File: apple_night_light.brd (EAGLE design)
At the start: 100 x 55 mm, 39 parts, among them U2 INA219AIDCNR, U3 ATSHA204-TSU, Y1 16MHZ

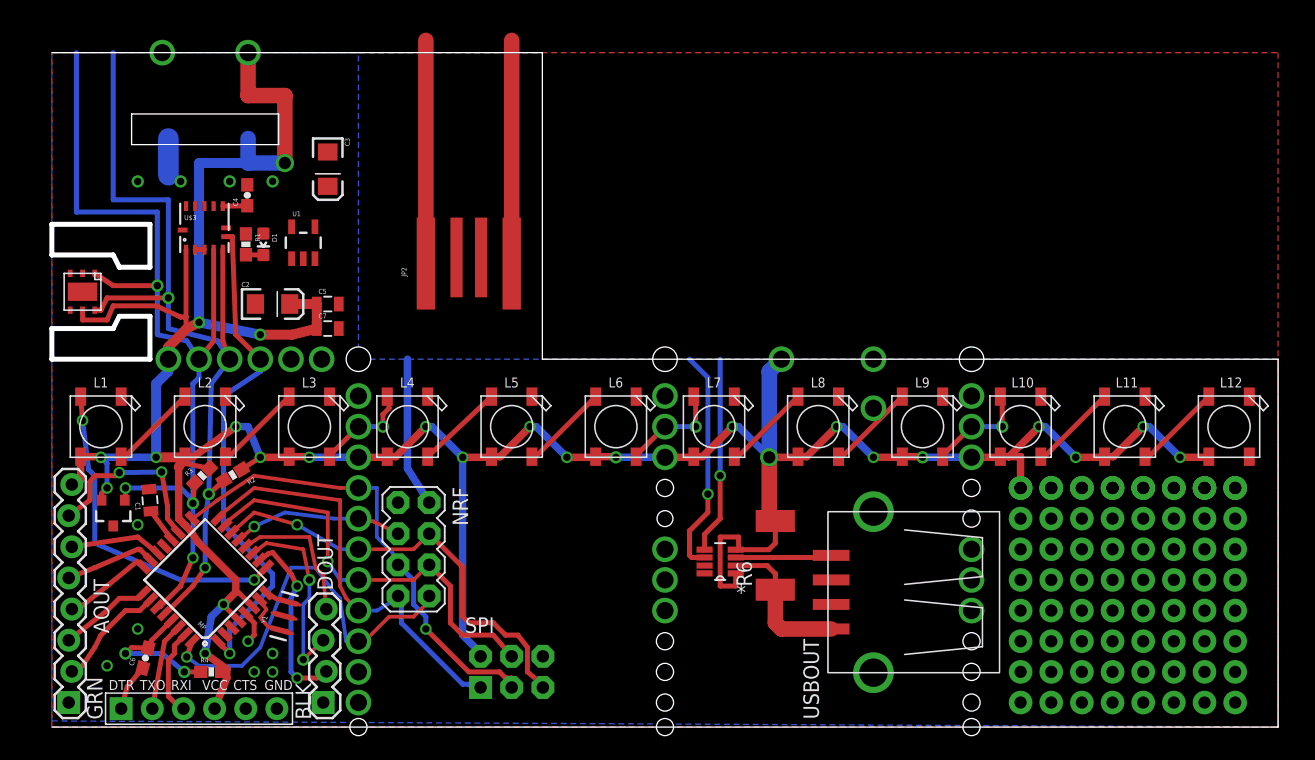
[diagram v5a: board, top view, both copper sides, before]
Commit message: layout power, move usb connector to save money, trying to finalize
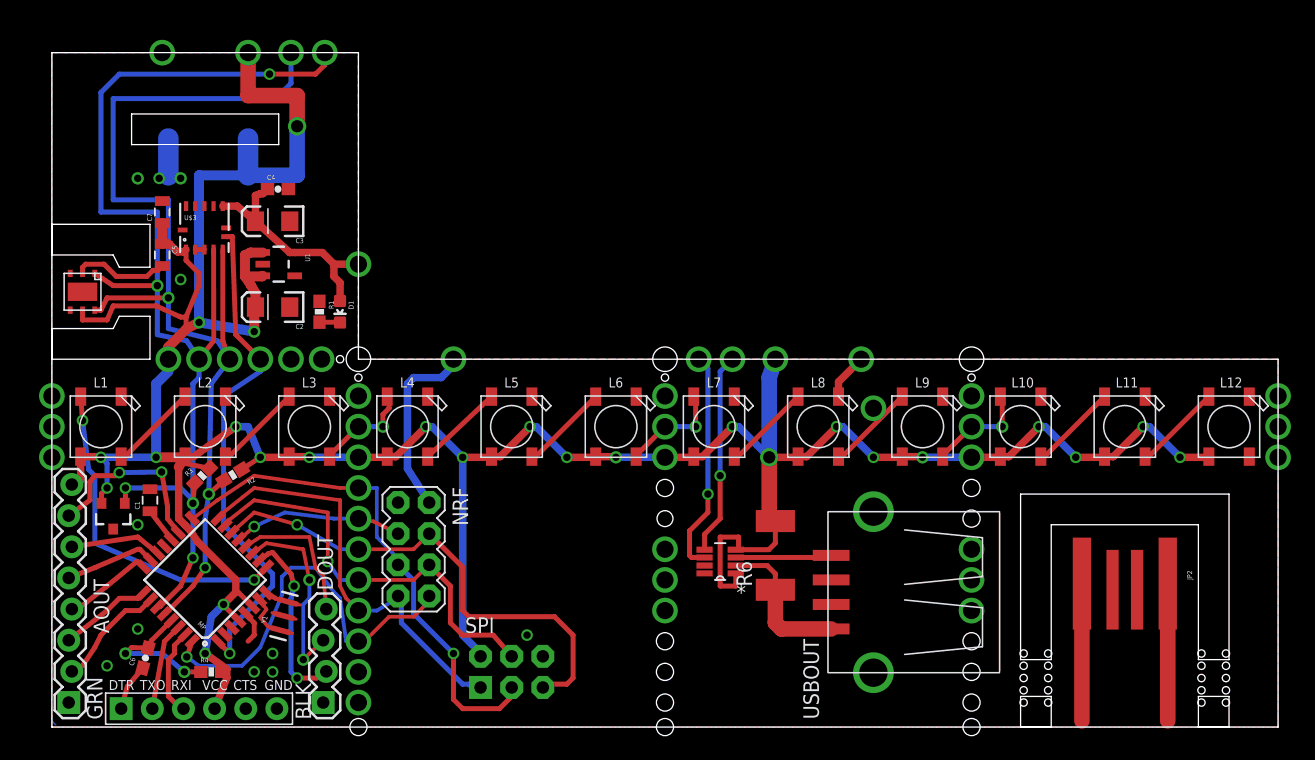
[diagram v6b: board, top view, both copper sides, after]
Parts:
- moved JP2 59.7 mm to (87.5, 11.5), turned to 270 degrees
- moved C7 16.5 mm to (9.00, 42.0), turned to 90 degrees
- moved C5 14.1 mm to (9.00, 38.5), turned to 270 degrees
- moved D1 8.33 mm to (23.5, 33.9)
- moved R1 8.14 mm to (21.8, 33.9)
- moved C3 6.19 mm to (18.0, 41.2), turned to 180 degrees
- moved U1 2.66 mm to (18.5, 37.8), turned to 270 degrees
- moved C4 2.55 mm to (18.4, 43.9), turned to 0 degrees
- moved C2 0.25 mm to (18.0, 34.2), turned to 180 degrees
- moved U3 0.25 mm to (5.00, 17.2)
- turned C1 to 90 degrees
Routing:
- net +3V3: track 14.2 -> 34.4 mm, vias 0 -> 2
- net SDA: track 97.5 -> 112.4 mm, vias 6 -> 9
- net SCL: track 88.9 -> 103.1 mm, vias 5 -> 7
- net CSN: track 36.1 -> 41.4 mm
- net GND: track 32.7 -> 37.4 mm, vias 33 -> 32
- net SCK: track 38.7 -> 42.2 mm
- net +5V: track 291.4 -> 288.5 mm, vias 33 -> 31
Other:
- outline, holes or cut-outs redrawn

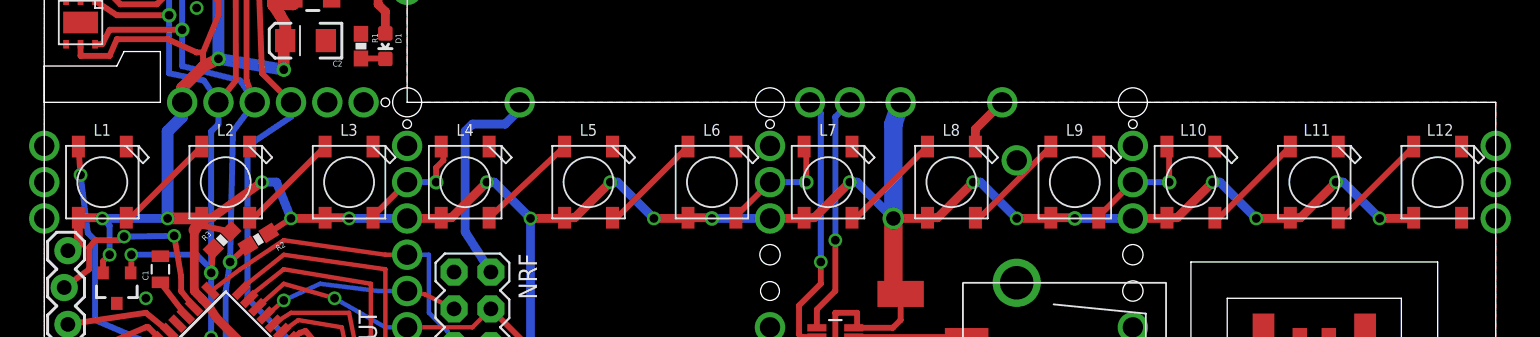
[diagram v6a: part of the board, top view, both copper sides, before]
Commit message: converting to dotstar LEDs, still some hookup work needed
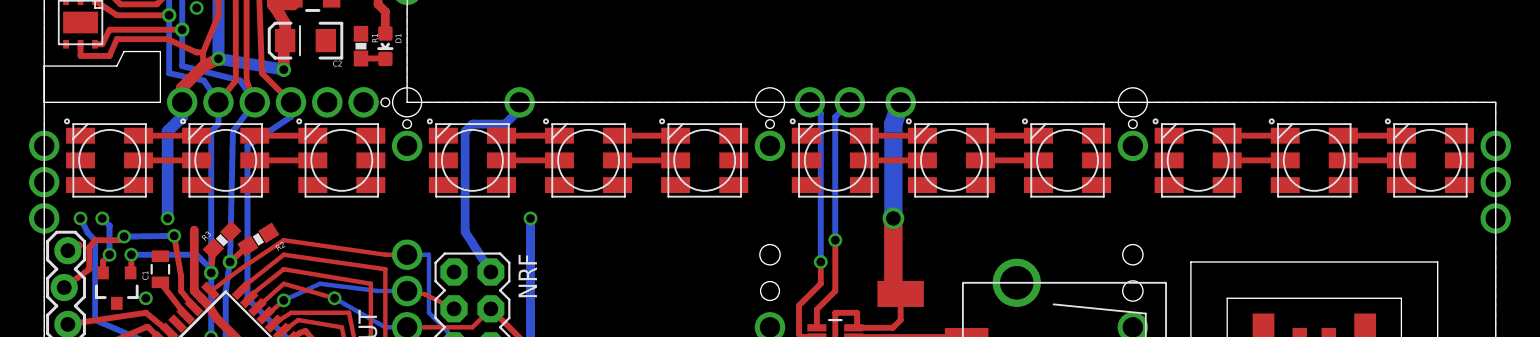
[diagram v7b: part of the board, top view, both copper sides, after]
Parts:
- removed L1, L10, L11, L12, L2, L3, L4, L5, L6, L7, L8, L9: WS2812B, adafruit:WS2812B
- added LED1, LED10, LED11, LED12, LED2, LED3, LED4, LED5, LED6, LED7, LED8, LED9: RGBLED5050, adafruit:RGBLED5050
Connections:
- removed net N$14: L5.2-DOUT, L6.4-DIN
- removed net N$20: L7.2-DOUT, L8.4-DIN
- removed net N$28: L4.2-DOUT, L5.4-DIN
- new net APACI: LED1.5
- new net APACI1: LED3.2, LED4.5
- new net APACI2: LED6.2, LED7.5
- new net APACI3: LED10.5, LED9.2
- new net APADI: LED1.4
- new net N$1: LED1.2, LED2.5
- new net N$15: LED4.2, LED5.5
- new net N$18: LED4.3, LED5.4
- new net N$26: LED8.3, LED9.4
- new net N$30: LED10.2, LED11.5
- new net N$31: LED11.2, LED12.5
- new net N$32: LED10.3, LED11.4
- new net N$35: LED11.3, LED12.4
- new net N$5: LED2.3, LED3.4
- new net N$6: LED3.3, LED4.4
- new net N$8: LED6.3, LED7.4
- net +5V: now also LED1.1, LED10.1, LED11.1, LED12.1, LED2.1, LED3.1, LED4.1, LED5.1, LED6.1, LED7.1, LED8.1, LED9.1; no longer L1.1-VDD, L10.1-VDD, L11.1-VDD, L12.1-VDD, L2.1-VDD, L3.1-VDD, L4.1-VDD, L5.1-VDD, L6.1-VDD, L7.1-VDD, L8.1-VDD, L9.1-VDD
- net GND: now also LED1.6, LED10.6, LED11.6, LED12.6, LED2.6, LED3.6, LED4.6, LED5.6, LED6.6, LED7.6, LED8.6, LED9.6; no longer L1.3-GND, L10.3-GND, L11.3-GND, L12.3-GND, L2.3-GND, L3.3-GND, L4.3-GND, L5.3-GND, L6.3-GND, L7.3-GND, L8.3-GND, L9.3-GND
- net N$12: now also LED10.4, LED9.3; no longer L6.2-DOUT, L7.4-DIN
- net N$17: now also LED5.2, LED6.5; no longer L10.4-DIN, L9.2-DOUT
- net N$19: now also LED5.3, LED6.4; no longer L8.2-DOUT, L9.4-DIN
- net N$2: now also LED2.2, LED3.5; no longer L2.2-DOUT, L3.4-DIN
- net N$23: now also LED7.2, LED8.5; no longer L3.2-DOUT, L4.4-DIN
- net N$24: now also LED8.2, LED9.5; no longer L11.2-DOUT, L12.4-DIN
- net N$25: now also LED7.3, LED8.4; no longer L10.2-DOUT, L11.4-DIN
- net N$3: now also LED1.3, LED2.4; no longer L1.2-DOUT, L2.4-DIN
- net NPIN: no longer L1.4-DIN
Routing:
- net +5V: track 288.5 -> 173.8 mm, vias 31 -> 13
- net N$12: track 8.49 -> 0.00 mm, vias 2 -> 0
- net N$20: track 7.23 -> 0.00 mm
- net N$14: track 7.23 -> 0.00 mm
- net N$28: track 7.14 -> 0.00 mm
- net NPIN: track 27.3 -> 22.4 mm
- net N$17: track 8.64 -> 4.00 mm, vias 2 -> 0
- net N$23: track 8.14 -> 4.00 mm, vias 2 -> 0
- net N$5: track 0.00 -> 4.00 mm
- net N$35: track 0.00 -> 4.00 mm
- net N$32: track 0.00 -> 4.00 mm
- net N$31: track 0.00 -> 4.00 mm
- net N$30: track 0.00 -> 4.00 mm
- net N$26: track 0.00 -> 4.00 mm
- net N$18: track 0.00 -> 4.00 mm
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
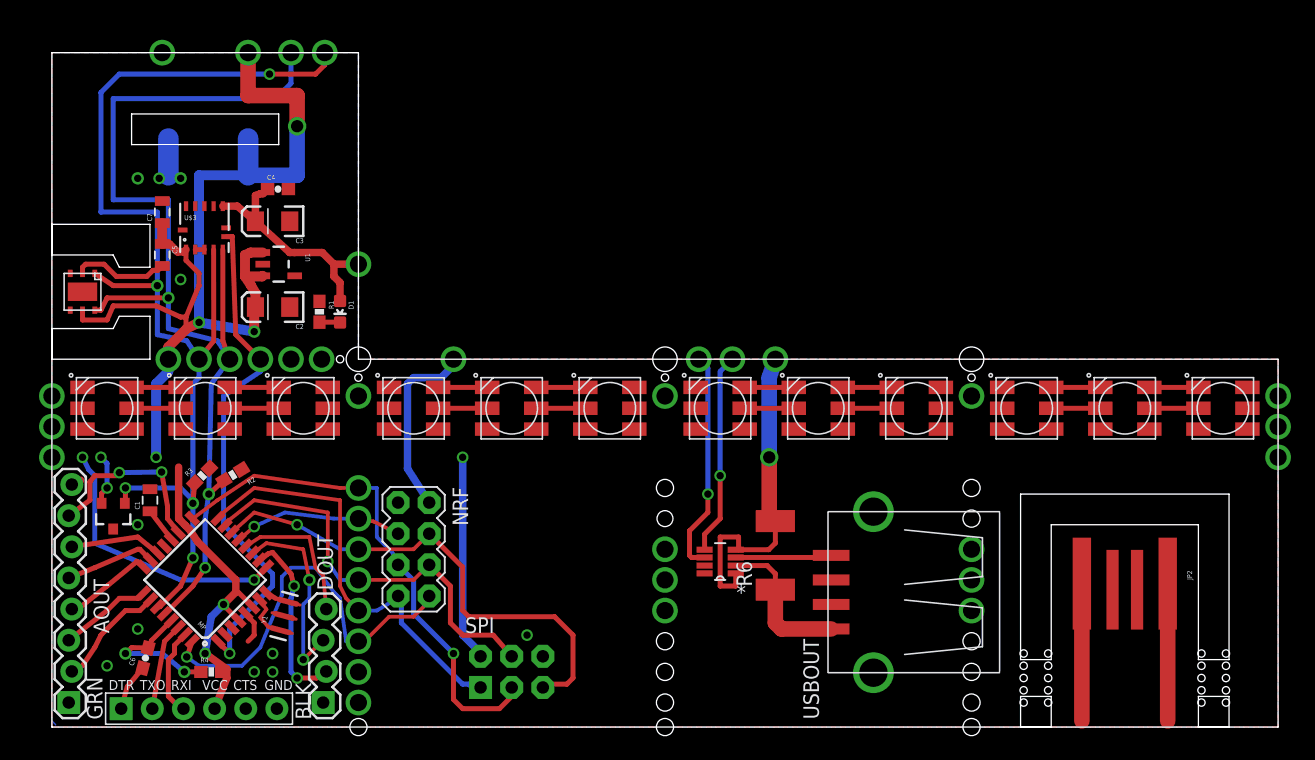
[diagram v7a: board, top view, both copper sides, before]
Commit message: more work on dotstar routing
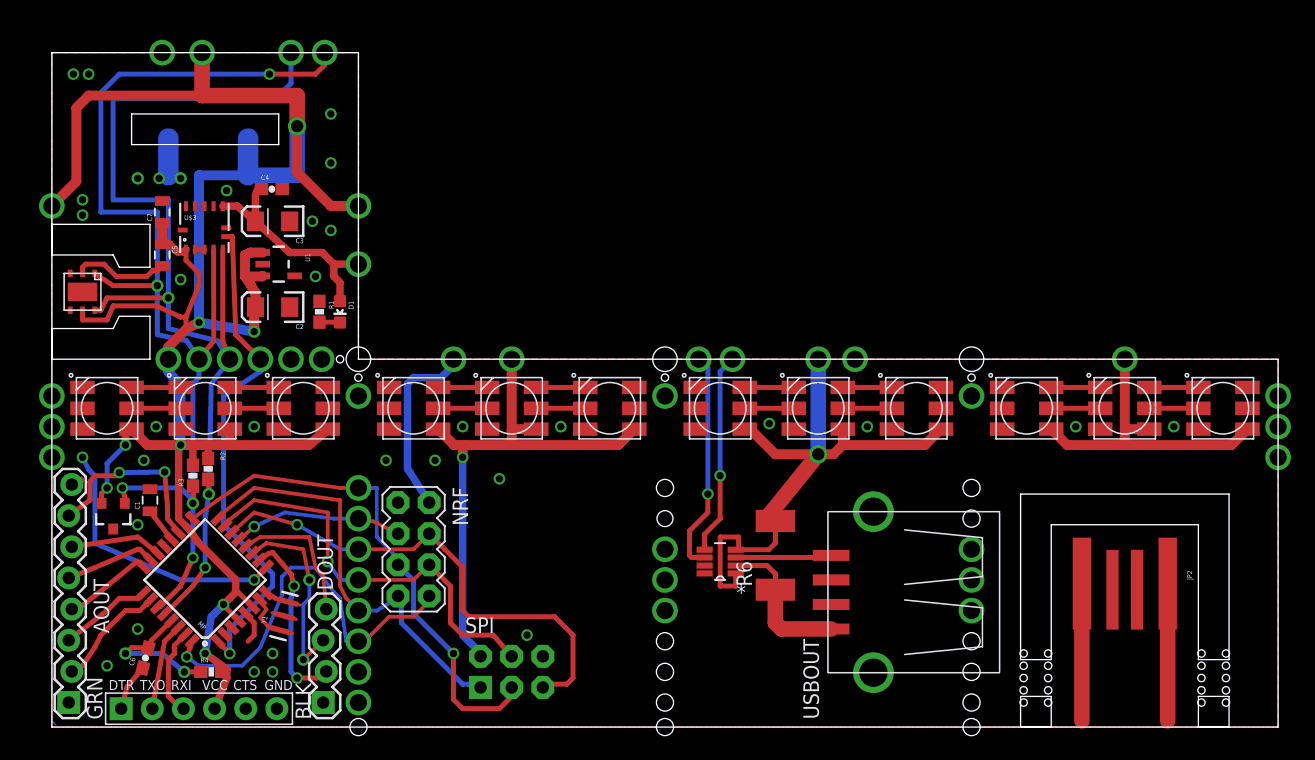
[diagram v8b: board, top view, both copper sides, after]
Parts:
- moved R2 2.06 mm to (12.8, 21.1), turned to 90 degrees
- moved R3 0.75 mm to (11.5, 20.5), turned to 90 degrees
- moved C4 0.50 mm to (17.9, 43.9)
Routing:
- net +5V: track 173.8 -> 304.3 mm, vias 13 -> 17
- net GND: vias 31 -> 54
